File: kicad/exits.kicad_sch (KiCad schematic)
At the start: 66 parts, among them IC1 NJM4556AV-TE1, IC2 NJM4556AV-TE1, J1 PJ301M12, J10 Conn_01x04_Female, J11 Conn_01x04_Male, J12 Conn_02x05_Odd_Even, J13 SJ-63083A, J14 SJ-63083A, J2 PJ301M12, J3 PJ301M12, J4 PJ301M12, J5 PJ301M12, J6 PJ301M12, J7 PJ301M12, J8 Conn_01x03_Male, J9 Conn_01x03_Female, U3 LME49720, U4 LME49720

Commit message: Add files via upload
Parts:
- J10: value Conn_01x04_Female -> Conn_01x06_Female
- J11: value Conn_01x04_Male -> Conn_01x06_Male
- J12: value Conn_02x05_Odd_Even -> Euro power header
- J8: value Conn_01x03_Male -> Conn_01x04_Male
- J9: value Conn_01x03_Female -> Conn_01x04_Female
- R11, R4: value 439k -> 442k
- R12, R3: value 103k -> 102k
- R13, R2: value 1M67 -> 1M69
- R7, R8: value 141k -> 140k
- RV1: value R_POT_Dual_Separate -> 50k A
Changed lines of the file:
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@@
     (in_bom yes) (on_board yes)
     (property "Reference" "R2" (id 0) (at 48.514 24.638 90))
-    (property "Value" "1M67" (id 1) (at 48.514 26.67 90))
+    (property "Value" "1M69" (id 1) (at 48.514 26.67 90))
     (property "Footprint" "nearness:0603" (id 2) (at 48.514 28.448 90)
       (effects (font (size 1.27 1.27)) hide)
@@
     (in_bom yes) (on_board yes)
     (property "Reference" "R3" (id 0) (at 48.514 39.878 90))
-    (property "Value" "103k" (id 1) (at 48.514 41.91 90))
+    (property "Value" "102k" (id 1) (at 48.514 41.91 90))
     (property "Footprint" "nearness:0603" (id 2) (at 48.514 43.688 90)
       (effects (font (size 1.27 1.27)) hide)
@@
     (in_bom yes) (on_board yes)
     (property "Reference" "R4" (id 0) (at 48.514 44.958 90))
-    (property "Value" "439k" (id 1) (at 48.514 46.99 90))
+    (property "Value" "442k" (id 1) (at 48.514 46.99 90))
     (property "Footprint" "nearness:0603" (id 2) (at 48.514 48.768 90)
       (effects (font (size 1.27 1.27)) hide)
@@
     (in_bom yes) (on_board yes)
     (property "Reference" "R7" (id 0) (at 48.514 80.518 90))
-    (property "Value" "141k" (id 1) (at 48.514 82.55 90))
+    (property "Value" "140k" (id 1) (at 48.514 82.55 90))
     (property "Footprint" "nearness:0603" (id 2) (at 48.514 84.328 90)
       (effects (font (size 1.27 1.27)) hide)
@@
     (in_bom yes) (on_board yes)
     (property "Reference" "R8" (id 0) (at 48.514 85.598 90))
-    (property "Value" "141k" (id 1) (at 48.514 87.63 90))
+    (property "Value" "140k" (id 1) (at 48.514 87.63 90))
     (property "Footprint" "nearness:0603" (id 2) (at 48.514 89.408 90)
       (effects (font (size 1.27 1.27)) hide)
@@
     (in_bom yes) (on_board yes)
     (property "Reference" "R11" (id 0) (at 48.514 121.158 90))
-    (property "Value" "439k" (id 1) (at 48.514 123.19 90))
+    (property "Value" "442k" (id 1) (at 48.514 123.19 90))
     (property "Footprint" "nearness:0603" (id 2) (at 48.514 124.968 90)
       (effects (font (size 1.27 1.27)) hide)
@@
     (in_bom yes) (on_board yes)
     (property "Reference" "R12" (id 0) (at 48.514 126.238 90))
-    (property "Value" "103k" (id 1) (at 48.514 128.27 90))
+    (property "Value" "102k" (id 1) (at 48.514 128.27 90))
     (property "Footprint" "nearness:0603" (id 2) (at 48.514 130.048 90)
       (effects (font (size 1.27 1.27)) hide)
@@
     (in_bom yes) (on_board yes)
     (property "Reference" "R13" (id 0) (at 48.514 141.478 90))
-    (property "Value" "1M67" (id 1) (at 48.514 143.51 90))
+    (property "Value" "1M69" (id 1) (at 48.514 143.51 90))
     (property "Footprint" "nearness:0603" (id 2) (at 48.514 145.288 90)
       (effects (font (size 1.27 1.27)) hide)
@@
     (in_bom yes) (on_board yes)
     (property "Reference" "J12" (id 0) (at 220.726 48.9458 0))
-    (property "Value" "Conn_02x05_Odd_Even" (id 1) (at 220.726 46.6344 0))
+    (property "Value" "Euro power header" (id 1) (at 220.726 46.6344 0))
     (property "Footprint" "Connector_IDC:IDC-Header_2x05_P2.54mm_Vertical" (id 2) (at 221.996 38.354 0)
       (effects (font (size 1.27 1.27)) hide)
@@
       (effects (font (size 1.27 1.27)) (justify right))
     )
-    (property "Value" "R_POT_Dual_Separate" (id 1) (at 60.706 161.925 0)
+    (property "Value" "50k A" (id 1) (at 60.706 161.925 0)
       (effects (font (size 1.27 1.27)) (justify right) hide)
     )
@@
       (effects (font (size 1.27 1.27)) (justify right))
     )
-    (property "Value" "R_POT_Dual_Separate" (id 1) (at 60.706 179.197 0)
+    (property "Value" "50k A" (id 1) (at 60.706 179.197 0)
       (effects (font (size 1.27 1.27)) (justify right) hide)
     )
@@
     (in_bom yes) (on_board yes)
     (property "Reference" "J8" (id 0) (at 95.25 72.644 0))
-    (property "Value" "Conn_01x03_Male" (id 1) (at 95.25 70.358 0)
+    (property "Value" "Conn_01x04_Male" (id 1) (at 95.25 70.358 0)
       (effects (font (size 1.27 1.27)) hide)
     )
@@
       (effects (font (size 1.27 1.27)) (justify left))
     )
-    (property "Value" "Conn_01x03_Female" (id 1) (at 64.008 70.358 0)
+    (property "Value" "Conn_01x04_Female" (id 1) (at 64.008 70.358 0)
       (effects (font (size 1.27 1.27)) (justify left) hide)
     )
@@
       (effects (font (size 1.27 1.27)) (justify left))
     )
-    (property "Value" "Conn_01x04_Female" (id 1) (at 87.0712 170.307 0)
+    (property "Value" "Conn_01x06_Female" (id 1) (at 87.0712 170.307 0)
       (effects (font (size 1.27 1.27)) (justify left) hide)
     )
@@
     (in_bom yes) (on_board yes)
     (property "Reference" "J11" (id 0) (at 89.662 161.036 0))
-    (property "Value" "Conn_01x04_Male" (id 1) (at 89.1032 162.56 0)
+    (property "Value" "Conn_01x06_Male" (id 1) (at 89.1032 162.56 0)
       (effects (font (size 1.27 1.27)) hide)
     )
@@
     )
     (path "/00000000-0000-0000-0000-000061cff58f"
-      (reference "J8") (unit 1) (value "Conn_01x03_Male") (footprint "Connector_PinHeader_2.54mm:PinHeader_1x04_P2.54mm_Vertical")
+      (reference "J8") (unit 1) (value "Conn_01x04_Male") (footprint "Connector_PinHeader_2.54mm:PinHeader_1x04_P2.54mm_Vertical")
     )
     (path "/00000000-0000-0000-0000-000061d06601"
-      (reference "J9") (unit 1) (value "Conn_01x03_Female") (footprint "Connector_PinSocket_2.54mm:PinSocket_1x04_P2.54mm_Vertical")
+      (reference "J9") (unit 1) (value "Conn_01x04_Female") (footprint "Connector_PinSocket_2.54mm:PinSocket_1x04_P2.54mm_Vertical")
     )
     (path "/00000000-0000-0000-0000-000061fd02f3"
-      (reference "J10") (unit 1) (value "Conn_01x04_Female") (footprint "Connector_PinSocket_2.54mm:PinSocket_1x06_P2.54mm_Vertical")
+      (reference "J10") (unit 1) (value "Conn_01x06_Female") (footprint "Connector_PinSocket_2.54mm:PinSocket_1x06_P2.54mm_Vertical")
     )
     (path "/00000000-0000-0000-0000-000061fe5a33"
-      (reference "J11") (unit 1) (value "Conn_01x04_Male") (footprint "Connector_PinHeader_2.54mm:PinHeader_1x06_P2.54mm_Vertical")
+      (reference "J11") (unit 1) (value "Conn_01x06_Male") (footprint "Connector_PinHeader_2.54mm:PinHeader_1x06_P2.54mm_Vertical")
     )
     (path "/00000000-0000-0000-0000-0000616d69c3"
-      (reference "J12") (unit 1) (value "Conn_02x05_Odd_Even") (footprint "Connector_IDC:IDC-Header_2x05_P2.54mm_Vertical")
+      (reference "J12") (unit 1) (value "Euro power header") (footprint "Connector_IDC:IDC-Header_2x05_P2.54mm_Vertical")
     )
     (path "/38f35b13-35ef-4f16-afff-0c07add69a73"
@@
     )
     (path "/00000000-0000-0000-0000-000058fd7e0e"
-      (reference "R2") (unit 1) (value "1M67") (footprint "nearness:0603")
+      (reference "R2") (unit 1) (value "1M69") (footprint "nearness:0603")
     )
     (path "/00000000-0000-0000-0000-000058fd7ef4"
-      (reference "R3") (unit 1) (value "103k") (footprint "nearness:0603")
+      (reference "R3") (unit 1) (value "102k") (footprint "nearness:0603")
     )
     (path "/00000000-0000-0000-0000-000058fd7efa"
-      (reference "R4") (unit 1) (value "439k") (footprint "nearness:0603")
+      (reference "R4") (unit 1) (value "442k") (footprint "nearness:0603")
     )
     (path "/00000000-0000-0000-0000-000058fd7fd6"
@@
     )
     (path "/00000000-0000-0000-0000-000058fd7fe2"
-      (reference "R7") (unit 1) (value "141k") (footprint "nearness:0603")
+      (reference "R7") (unit 1) (value "140k") (footprint "nearness:0603")
     )
     (path "/00000000-0000-0000-0000-000058fd7fe8"
-      (reference "R8") (unit 1) (value "141k") (footprint "nearness:0603")
+      (reference "R8") (unit 1) (value "140k") (footprint "nearness:0603")
     )
     (path "/00000000-0000-0000-0000-000058fd817a"
@@
     )
     (path "/00000000-0000-0000-0000-000058fd8186"
-      (reference "R11") (unit 1) (value "439k") (footprint "nearness:0603")
+      (reference "R11") (unit 1) (value "442k") (footprint "nearness:0603")
     )
     (path "/00000000-0000-0000-0000-000058fd818c"
-      (reference "R12") (unit 1) (value "103k") (footprint "nearness:0603")
+      (reference "R12") (unit 1) (value "102k") (footprint "nearness:0603")
     )
     (path "/00000000-0000-0000-0000-000058fd8192"
-      (reference "R13") (unit 1) (value "1M67") (footprint "nearness:0603")
+      (reference "R13") (unit 1) (value "1M69") (footprint "nearness:0603")
     )
     (path "/00000000-0000-0000-0000-000058fd8198"
@@
     )
     (path "/00000000-0000-0000-0000-000061bdd79d"
-      (reference "RV1") (unit 1) (value "R_POT_Dual_Separate") (footprint "Potentiometer_THT:Potentiometer_Alpha_RD902F-40-00D_Dual_Vertical")
+      (reference "RV1") (unit 1) (value "50k A") (footprint "Potentiometer_THT:Potentiometer_Alpha_RD902F-40-00D_Dual_Vertical")
     )
     (path "/00000000-0000-0000-0000-000061bdf4c9"
-      (reference "RV1") (unit 2) (value "R_POT_Dual_Separate") (footprint "Potentiometer_THT:Potentiometer_Alpha_RD902F-40-00D_Dual_Vertical")
+      (reference "RV1") (unit 2) (value "50k A") (footprint "Potentiometer_THT:Potentiometer_Alpha_RD902F-40-00D_Dual_Vertical")
     )
     (path "/00000000-0000-0000-0000-0000615939a4"

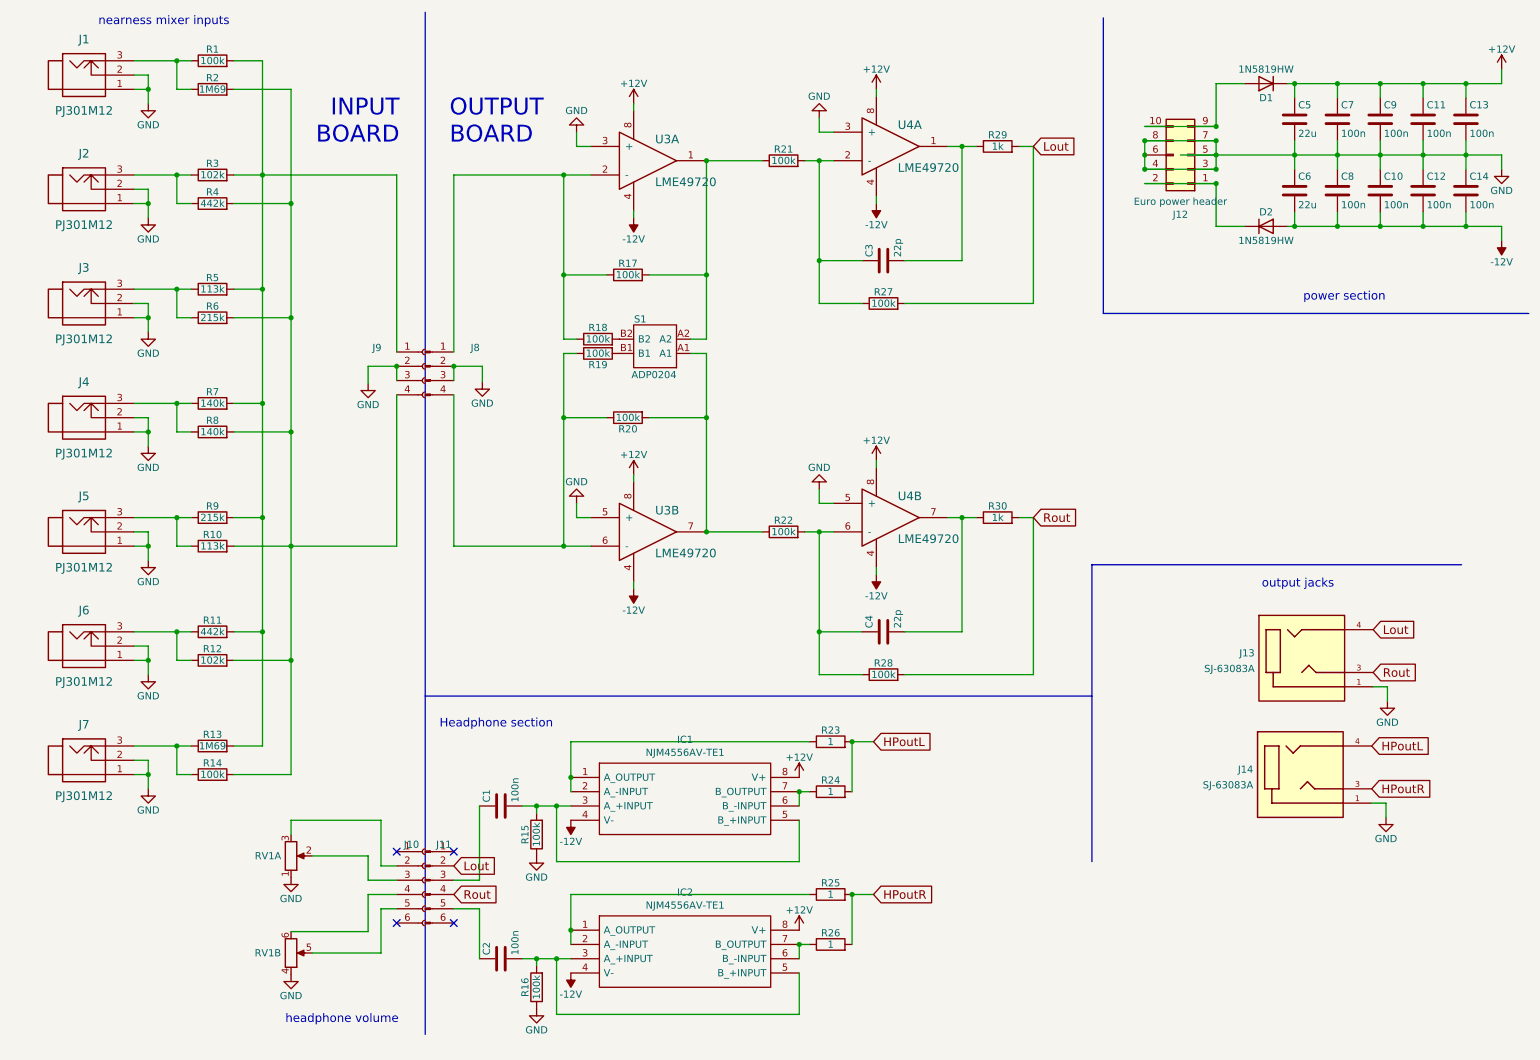
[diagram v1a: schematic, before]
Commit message: Switched to CMOY style hp out w RC4850, and added stereo panning
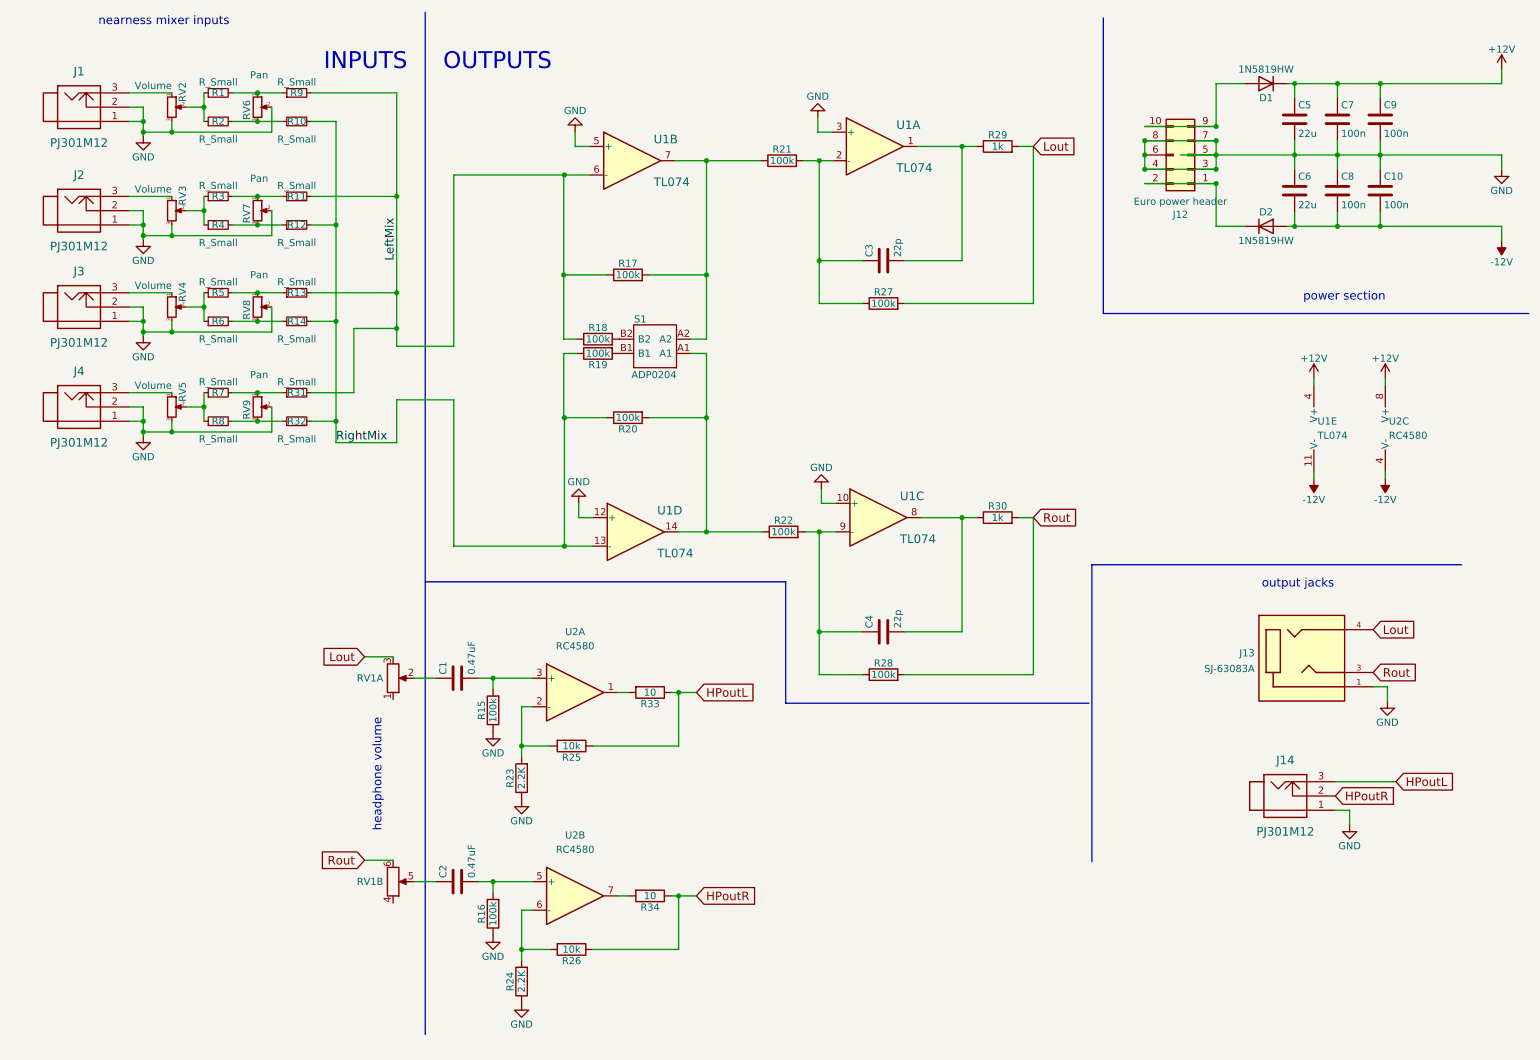
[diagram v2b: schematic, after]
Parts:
- removed C11, C12, C13, C14: 100n, nearness:0603, symbol Device:C
- removed IC1, IC2: NJM4556AV-TE1, SamacSys_Parts:SOP65P640X145-8N, symbol SamacSys_Parts:NJM4556AV-TE1
- removed J10: Conn_01x06_Female, Connector_PinSocket_2.54mm:PinSocket_1x06_P2.54mm_Vertical, symbol Connector:Conn_01x06_Female
- removed J11: Conn_01x06_Male, Connector_PinHeader_2.54mm:PinHeader_1x06_P2.54mm_Vertical, symbol Connector:Conn_01x06_Male
- removed J14: SJ-63083A, Connector:CUI_SJ-63083A, symbol SJ-63083A:SJ-63083A
- removed J5, J6, J7: PJ301M12, nearness:PJ301M12, symbol pj301m12:PJ301M12
- removed J8: Conn_01x04_Male, Connector_PinHeader_2.54mm:PinHeader_1x04_P2.54mm_Vertical, symbol Connector:Conn_01x04_Male
- removed J9: Conn_01x04_Female, Connector_PinSocket_2.54mm:PinSocket_1x04_P2.54mm_Vertical, symbol Connector:Conn_01x04_Female
- removed R1, R14: 100k, nearness:0603, symbol Device:R
- removed R10, R5: 113k, nearness:0603, symbol Device:R
- removed R11, R4: 442k, nearness:0603, symbol Device:R
- removed R12, R3: 102k, nearness:0603, symbol Device:R
- removed R13, R2: 1M69, nearness:0603, symbol Device:R
- removed R6, R9: 215k, nearness:0603, symbol Device:R
- removed R7, R8: 140k, nearness:0603, symbol Device:R
- added J14: PJ301M12, nearness:PJ301M12, symbol pj301m12:PJ301M12
- added R1, R10, R11, R12, R13, R14, R2, R3, R31, R32, R4, R5, R6, R7, R8, R9: R_Small, nearness:0603, symbol Device:R_Small
- added R33, R34: 10, Resistor_SMD:R_1206_3216Metric, symbol Device:R
- added RV2, RV3, RV4, RV5: Volume, Potentiometer_THT:Potentiometer_Alps_RK09K_Single_Vertical, symbol Device:R_Potentiometer_Small
- added RV6, RV7, RV8, RV9: Pan, Potentiometer_THT:Potentiometer_Alps_RK09K_Single_Vertical, symbol Device:R_Potentiometer_Small
- added unit 5 of U1
- added U2: RC4580, Package_SO:SOIC-8_3.9x4.9mm_P1.27mm, symbol Amplifier_Operational:RC4580
- C1, C2: value 100n -> 0.47uF; footprint Capacitors_SMD:C_1206 -> Capacitor_SMD:C_1206_3216Metric
- R23, R24: value 1 -> 2.2K
- R25, R26: value 1 -> 10k
- U1: renamed from U3; value LME49720 -> TL074; footprint nearness:SOIC-8 -> Package_SO:SOIC-14_3.9x8.7mm_P1.27mm; symbol lme49720:LME49720 -> Amplifier_Operational:TL074
- U1: renamed from U4; value LME49720 -> TL074; footprint nearness:SOIC-8 -> Package_SO:SOIC-14_3.9x8.7mm_P1.27mm; symbol lme49720:LME49720 -> Amplifier_Operational:TL074
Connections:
- net +12V: now also U1.4 (V+), U2.8 (V+); no longer U1.8, U1.8, U1.8, U1.8
- net -12V: now also U1.11 (V-), U2.4 (V-); no longer U1.4, U1.4, U1.4, U1.4
- net GND: now also R23.1, R24.1, U1.10 (+), U1.12 (+), U1.5 (+), J14.1, RV2.3, RV3.3, RV4.3, RV5.3, RV6.2, RV7.2, RV8.2, RV9.2; no longer RV1.1, RV1.4, U1.3 (+), U1.5 (+), U1.5 (+)
- net HPoutL: now also R25.1, J14.3, R33.1; no longer R23.2, R24.2
- net HPoutR: now also R26.1, J14.2, R34.1; no longer R25.2, R26.2
- net Lout: now also RV1.3
- net Rout: now also RV1.6
- net at J1.3: now also RV2.1
- net at J2.3: now also RV3.1
- net at J3.3: now also RV4.1
- net at J4.3: now also RV5.1
- net at C4.2, R30.1: now also U1.8; no longer U1.7
- net LeftMix: now reaches R17.1, R18.1
- net LeftMix: now also R11.2, R13.2, R31.2, R9.2; no longer U1.2 (-)
- net at R17.2, R21.1, S1.A2: now also U1.7; no longer U1.1
- net RightMix: now reaches R19.1, R20.1
- net RightMix: now also U1.13 (-), R10.2, R12.2, R14.2, R32.2; no longer U1.6 (-)
- net at R20.2, R22.1, S1.A1: now also U1.14; no longer U1.7
- net at C4.1, R22.2, R28.1: now also U1.9 (-); no longer U1.6 (-)
- net at C2.2, R16.2: now also U2.5 (+)
- net at C2.1: now also RV1.5
- net at C1.2, R15.2: now also U2.3 (+)
- net at C1.1: now also RV1.2
- new net: R3.1, R4.1, RV3.2
- new net: R10.1, R2.2, RV6.3
- new net: R1.1, R2.1, RV2.2
- new net: R11.1, R3.2, RV7.1
- new net: R1.2, R9.1, RV6.1
- new net: R7.1, R8.1, RV5.2
- new net: R31.1, R7.2, RV9.1
- new net: R13.1, R5.2, RV8.1
- new net: R32.1, R8.2, RV9.3
- new net: R12.1, R4.2, RV7.3
- new net: R5.1, R6.1, RV4.2
- new net: R14.1, R6.2, RV8.3
- new net: R24.2, R26.2, U2.6 (-)
- new net: R34.2, U2.7
- new net: R33.2, U2.1
- new net: R23.2, R25.2, U2.2 (-)
- no-connect marks 4 -> 0
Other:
- note added: "INPUTS"
- note added: "OUTPUTS"
- note removed: "Headphone section"
- note removed: "INPUT BOARD"
- note removed: "OUTPUT BOARD"

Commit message: add panel outline, tweak R values, dips -> headers
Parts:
- removed S1: ADP0204, SamacSys_Parts:ADP0204, symbol SamacSys_Parts:ADP0204
- added J5, J6: Attenuator Jumper 1, Connector_PinHeader_2.54mm:PinHeader_1x03_P2.54mm_Vertical, symbol Connector:Conn_01x03_Male
- R23, R24: value 2.2K -> 10K
- R25, R26: value 10k -> 1K
- R29, R30: value 1k -> 470
- RV1: value 50k A -> 50KA
- RV2, RV3, RV4, RV5: value Volume -> 50K
- RV6, RV7, RV8, RV9: value Pan -> 50K
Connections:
- net GND: now also RV1.1, RV1.4
- net at R17.2, R21.1, U1.7: now also J5.2 (Pin_2)
- net at R20.2, R22.1, U1.14: now also J6.2 (Pin_2)
- net at R18.2: now also J5.3 (Pin_3)
- net at R19.2: now also J6.1 (Pin_1)
- no-connect marks 0 -> 2
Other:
- note added: "These guys all need values"
- note added: "WHY ARE THERE TWO STAGES FOR EACH CHANNEL? My guess - inverting then inverting again?"
